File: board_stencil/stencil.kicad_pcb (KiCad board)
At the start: 2 copper layers, 285 x 185 mm, 117 parts, among them J1 USB_C_Receptacle_USB2.0, P1 USB_C_Plug, SW1 Reset, SW2 Next, SW3 Previous, SW4 boot, SW5 run, U1 AP2112K-3.3, U1 PCF8591, U2 PCF8591, U2 W25Q128JVS, U3 AP2112K-3.3, U3 PCF8591, U3 RP2040, U4 PCF8591, U8 SN74AHCT125QDRG4Q1, U9 PCF8591, Y1 ABLS-12.000MHZ-B4-T

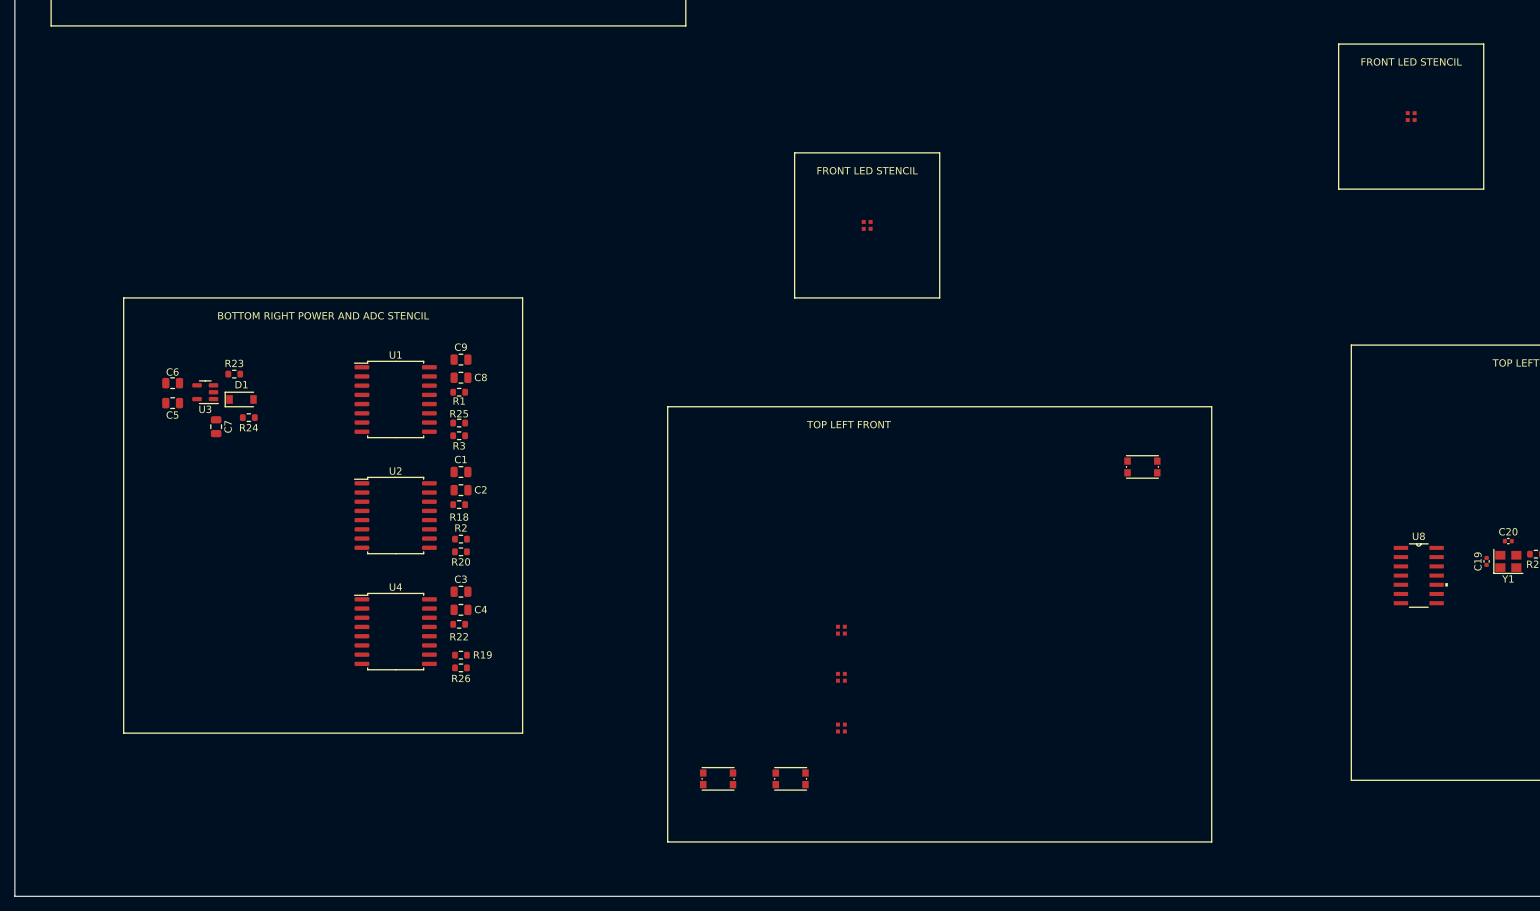
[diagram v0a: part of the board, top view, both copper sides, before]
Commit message: added some cutouts from another project to the stencil
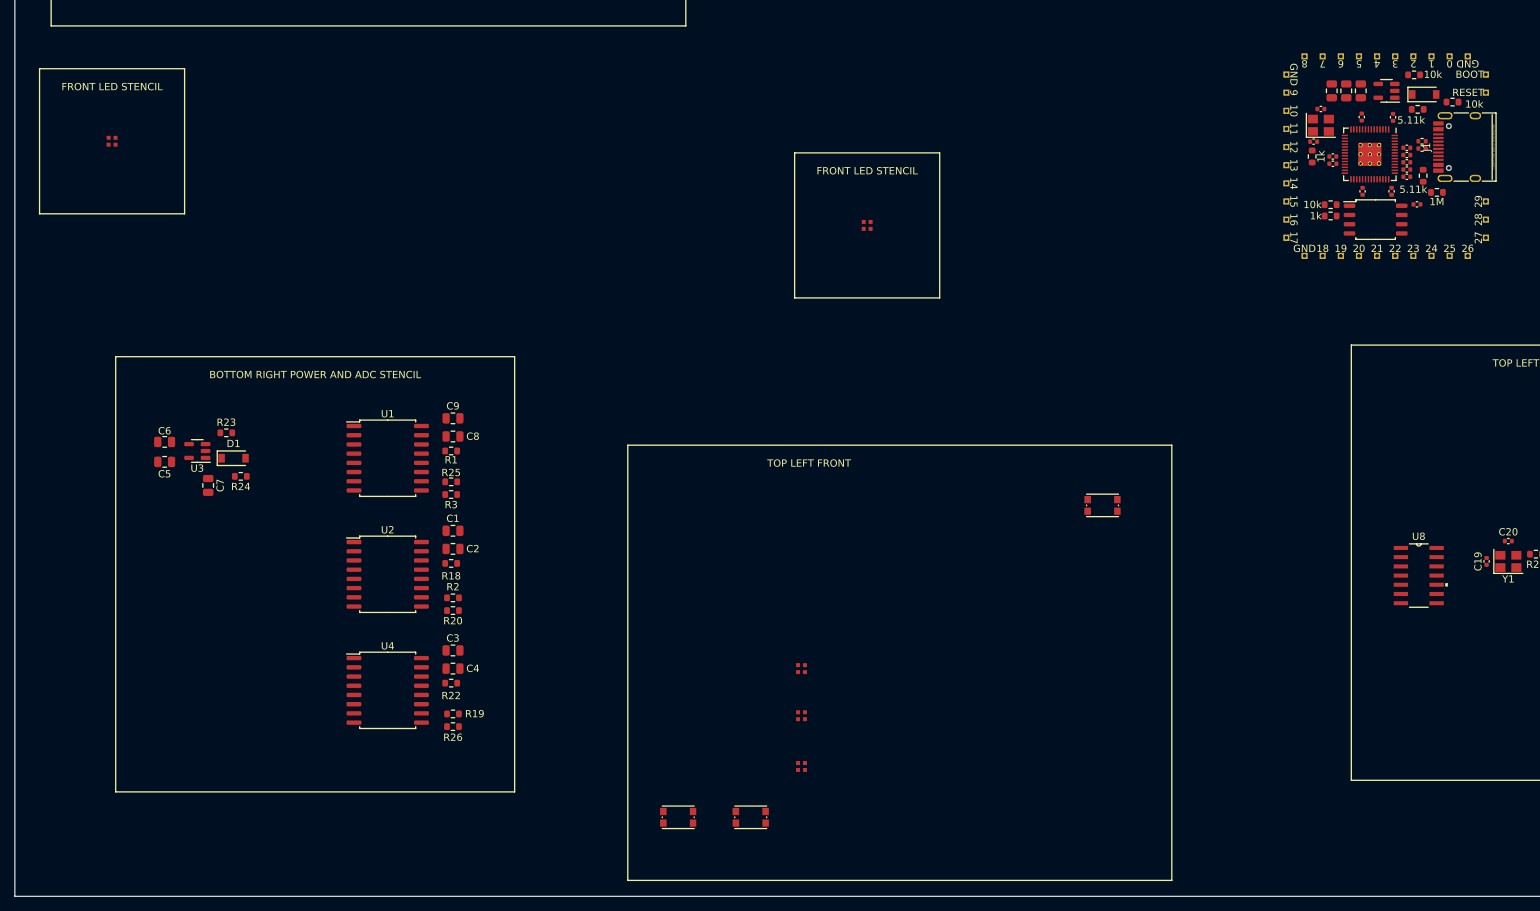
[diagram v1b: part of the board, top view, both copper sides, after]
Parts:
- added 0: MountingHole_Pad, dip:PinHeader_1x01_P1.00mm_Vertical, F.Cu at (217.8, 89.2)
- added 1: MountingHole_Pad, dip:PinHeader_1x01_P1.00mm_Vertical, F.Cu at (215.3, 89.2)
- added 10: MountingHole_Pad, dip:PinHeader_1x01_P1.00mm_Vertical, F.Cu at (195.3, 96.7)
- added 11: MountingHole_Pad, dip:PinHeader_1x01_P1.00mm_Vertical, F.Cu at (195.3, 99.2)
- added 12: MountingHole_Pad, dip:PinHeader_1x01_P1.00mm_Vertical, F.Cu at (195.3, 101.7)
- added 13: MountingHole_Pad, dip:PinHeader_1x01_P1.00mm_Vertical, F.Cu at (195.3, 104.2)
- added 14: MountingHole_Pad, dip:PinHeader_1x01_P1.00mm_Vertical, F.Cu at (195.3, 106.7)
- added 15: MountingHole_Pad, dip:PinHeader_1x01_P1.00mm_Vertical, F.Cu at (195.3, 109.2)
- added 16: MountingHole_Pad, dip:PinHeader_1x01_P1.00mm_Vertical, F.Cu at (195.3, 111.7)
- added 17: MountingHole_Pad, dip:PinHeader_1x01_P1.00mm_Vertical, F.Cu at (195.3, 114.2)
- added 18: MountingHole_Pad, dip:PinHeader_1x01_P1.00mm_Vertical, F.Cu at (200.3, 116.7)
- added 19: MountingHole_Pad, dip:PinHeader_1x01_P1.00mm_Vertical, F.Cu at (202.8, 116.7)
- added 2: MountingHole_Pad, dip:PinHeader_1x01_P1.00mm_Vertical, F.Cu at (212.8, 89.2)
- added 20: MountingHole_Pad, dip:PinHeader_1x01_P1.00mm_Vertical, F.Cu at (205.3, 116.7)
- added 21: MountingHole_Pad, dip:PinHeader_1x01_P1.00mm_Vertical, F.Cu at (207.8, 116.7)
- added 22: MountingHole_Pad, dip:PinHeader_1x01_P1.00mm_Vertical, F.Cu at (210.3, 116.7)
- added 23: MountingHole_Pad, dip:PinHeader_1x01_P1.00mm_Vertical, F.Cu at (212.8, 116.7)
- added 24: MountingHole_Pad, dip:PinHeader_1x01_P1.00mm_Vertical, F.Cu at (215.3, 116.7)
- added 25: MountingHole_Pad, dip:PinHeader_1x01_P1.00mm_Vertical, F.Cu at (217.8, 116.7)
- added 26: MountingHole_Pad, dip:PinHeader_1x01_P1.00mm_Vertical, F.Cu at (220.3, 116.7)
- added 27: MountingHole_Pad, dip:PinHeader_1x01_P1.00mm_Vertical, F.Cu at (222.8, 114.2)
- added 28: MountingHole_Pad, dip:PinHeader_1x01_P1.00mm_Vertical, F.Cu at (222.8, 111.7)
- added 29: MountingHole_Pad, dip:PinHeader_1x01_P1.00mm_Vertical, F.Cu at (222.8, 109.2)
- added 3: MountingHole_Pad, dip:PinHeader_1x01_P1.00mm_Vertical, F.Cu at (210.3, 89.2)
- added 4: MountingHole_Pad, dip:PinHeader_1x01_P1.00mm_Vertical, F.Cu at (207.8, 89.2)
- added 5: MountingHole_Pad, dip:PinHeader_1x01_P1.00mm_Vertical, F.Cu at (205.3, 89.2)
- added 6: MountingHole_Pad, dip:PinHeader_1x01_P1.00mm_Vertical, F.Cu at (202.8, 89.2)
- added 7: MountingHole_Pad, dip:PinHeader_1x01_P1.00mm_Vertical, F.Cu at (200.3, 89.2)
- added 8: MountingHole_Pad, dip:PinHeader_1x01_P1.00mm_Vertical, F.Cu at (197.8, 89.2)
- added 9: MountingHole_Pad, dip:PinHeader_1x01_P1.00mm_Vertical, F.Cu at (195.3, 94.2)
- added BOOT: MountingHole_Pad, dip:PinHeader_1x01_P1.00mm_Vertical, F.Cu at (222.8, 91.7)
- added C1: 100n, Capacitor_SMD:C_0402_1005Metric, F.Cu at (201.7, 104.0)
- added C10: 10u, Capacitor_SMD:C_0805_2012Metric, F.Cu at (203.6, 94.0)
- added C11: 10u, Capacitor_SMD:C_0805_2012Metric, F.Cu at (201.6, 94.0)
- added C12: 10u, Capacitor_SMD:C_0805_2012Metric, F.Cu at (205.6, 94.0)
- added C13: 1u, Capacitor_SMD:C_0402_1005Metric, F.Cu at (211.9, 103.8)
- added C14: 1u, Capacitor_SMD:C_0402_1005Metric, F.Cu at (211.9, 105.8)
- added C15: 100n, Capacitor_SMD:C_0402_1005Metric, F.Cu at (213.3, 109.6)
- added C16: 27p, Capacitor_SMD:C_0402_1005Metric, F.Cu at (200.1, 96.5)
- added C17: 27p, Capacitor_SMD:C_0402_1005Metric, F.Cu at (199.1, 101.0)
- added C2: 100n, Capacitor_SMD:C_0402_1005Metric, F.Cu at (211.9, 101.8)
- added C3: 100n, Capacitor_SMD:C_0402_1005Metric, F.Cu at (209.8, 107.8)
- added C4: 100n, Capacitor_SMD:C_0402_1005Metric, F.Cu at (211.9, 102.8)
- added C5: 100n, Capacitor_SMD:C_0402_1005Metric, F.Cu at (211.9, 104.8)
- added C6: 100n, Capacitor_SMD:C_0402_1005Metric, F.Cu at (210.0, 97.6)
- added C7: 100n, Capacitor_SMD:C_0402_1005Metric, F.Cu at (205.7, 97.6)
- added C8: 100n, Capacitor_SMD:C_0402_1005Metric, F.Cu at (201.7, 103.0)
- added C9: 100n, Capacitor_SMD:C_0402_1005Metric, F.Cu at (205.8, 107.8)
- added D1: MBR0540, Diode_SMD:D_SOD-123, F.Cu at (214.3, 94.5)
- added GND: MountingHole_Pad, dip:PinHeader_1x01_P1.00mm_Vertical, F.Cu at (197.8, 116.7)
- added GND: MountingHole_Pad, dip:PinHeader_1x01_P1.00mm_Vertical, F.Cu at (220.3, 89.2)
- added GND: MountingHole_Pad, dip:PinHeader_1x01_P1.00mm_Vertical, F.Cu at (195.3, 91.7)
- added J1: USB_C_Receptacle_USB2.0, dip:USB_C_Receptacle_HRO_TYPE-C-31-M-12_PASTE, F.Cu at (220.3, 101.7)
- added R1: 10k, Resistor_SMD:R_0603_1608Metric, F.Cu at (212.9, 91.8)
- added R10: 1k, Resistor_SMD:R_0603_1608Metric, F.Cu at (198.8, 103.0)
- added R2: 10k, Resistor_SMD:R_0603_1608Metric, F.Cu at (218.2, 95.5)
- added R3: 27, Resistor_SMD:R_0402_1005Metric, F.Cu at (214.0, 100.9)
- added R4: 27, Resistor_SMD:R_0402_1005Metric, F.Cu at (214.0, 101.9)
- added R5: 5.11k, Resistor_SMD:R_0603_1608Metric, F.Cu at (214.2, 105.7)
- added R6: 5.11k, Resistor_SMD:R_0603_1608Metric, F.Cu at (213.4, 96.5)
- added R7: 1M, Resistor_SMD:R_0603_1608Metric, F.Cu at (216.1, 108.0)
- added R8: 10k, Resistor_SMD:R_0603_1608Metric, F.Cu at (201.4, 109.7)
- added R9: 1k, Resistor_SMD:R_0603_1608Metric, F.Cu at (201.4, 111.2)
- added RESET: MountingHole_Pad, dip:PinHeader_1x01_P1.00mm_Vertical, F.Cu at (222.8, 94.2)
- added U1: AP2112K-3.3, Package_TO_SOT_SMD:SOT-23-5, F.Cu at (209.1, 94.0)
- added U2: RP2040, RP2040_minimal:RP2040-QFN-56, F.Cu at (206.8, 102.7)
- added U3: W25Q128JVS, Package_SO:SOIC-8_5.23x5.23mm_P1.27mm, F.Cu at (207.6, 111.7)
- added Y1: Crystal_GND24, Crystal:Crystal_SMD_3225-4Pin_3.2x2.5mm, F.Cu at (200.1, 98.7)
- moved D3 179.1 mm to (33.4, 100.9)
- moved C1 8.17 mm to (80.4, 154.6)
- moved C2 8.17 mm to (80.4, 157.1)
- moved C3 8.17 mm to (80.4, 171.1)
- moved C4 8.17 mm to (80.4, 173.6)
- moved C5 8.17 mm to (40.6, 145.1)
- moved C6 8.17 mm to (40.6, 142.3)
- moved C7 8.17 mm to (46.6, 148.3)
- moved C8 8.17 mm to (80.4, 141.6)
- moved C9 8.17 mm to (80.4, 139.1)
- moved D1 8.17 mm to (50.1, 144.6)
- moved R1 8.17 mm to (80.2, 143.6)
- moved R18 8.17 mm to (80.2, 159.1)
- moved R19 8.17 mm to (80.4, 179.8)
- moved R2 8.17 mm to (80.4, 163.8)
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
